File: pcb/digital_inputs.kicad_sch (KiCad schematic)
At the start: 9 parts, among them CN3 VL0831510000G, U2 ISO1212, U4 ISO1212

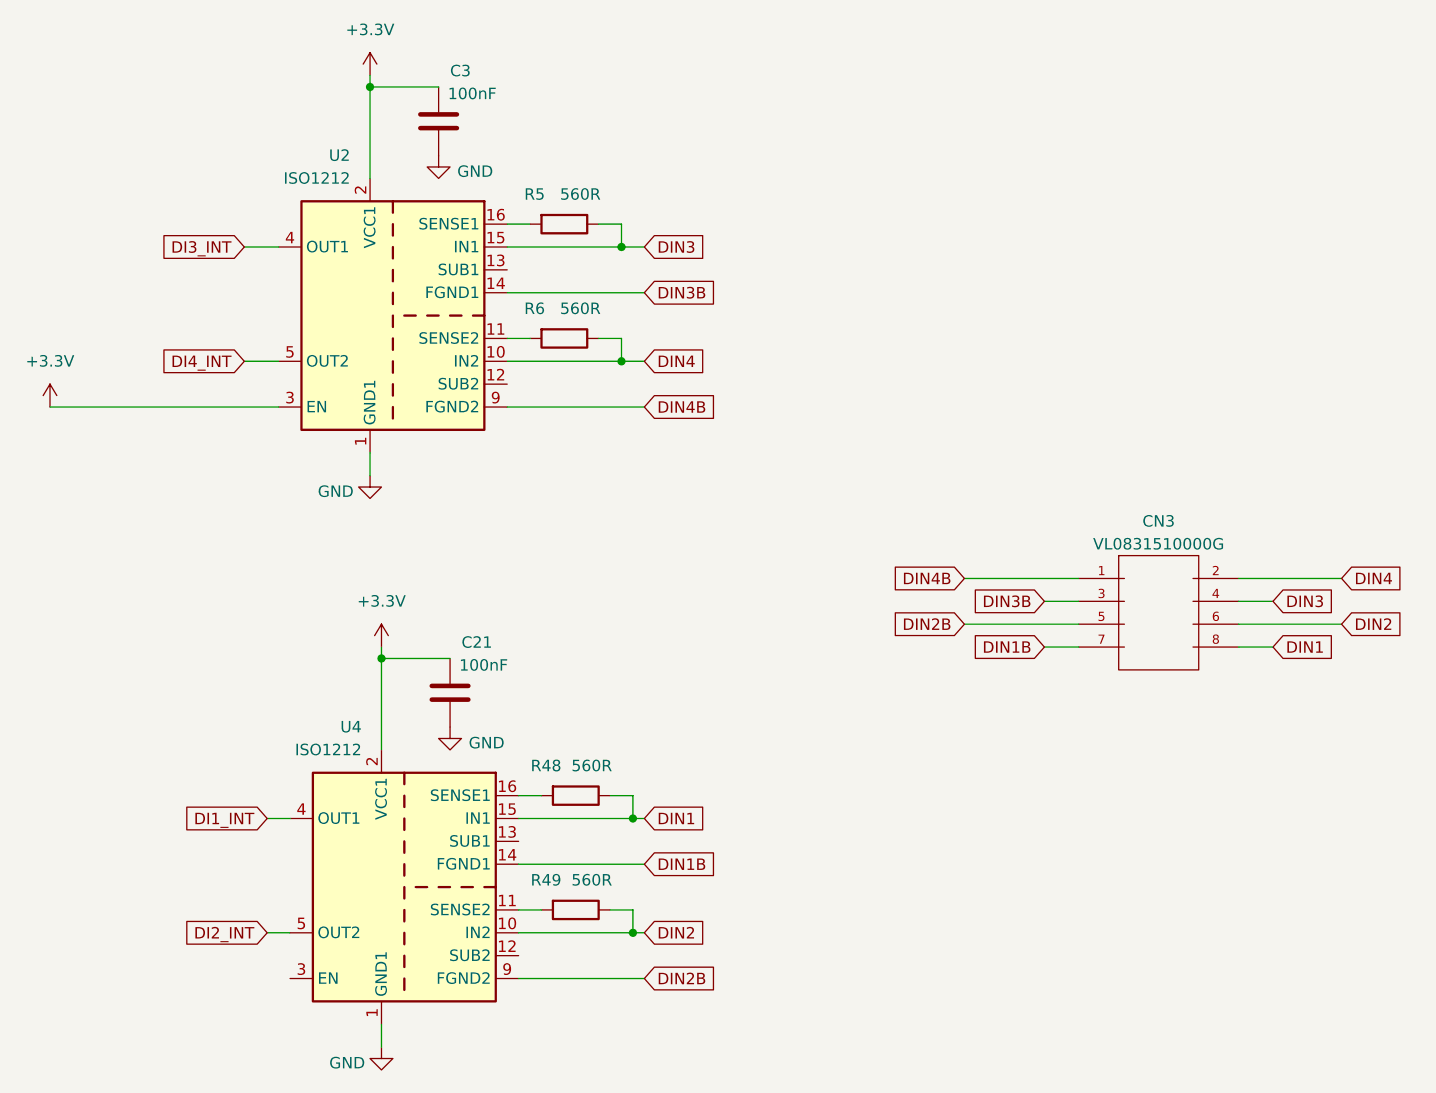
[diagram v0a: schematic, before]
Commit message: Added recommended threshold resistor and capacitor to all digital inputs, as recommended in the ISO1212 datasheet.
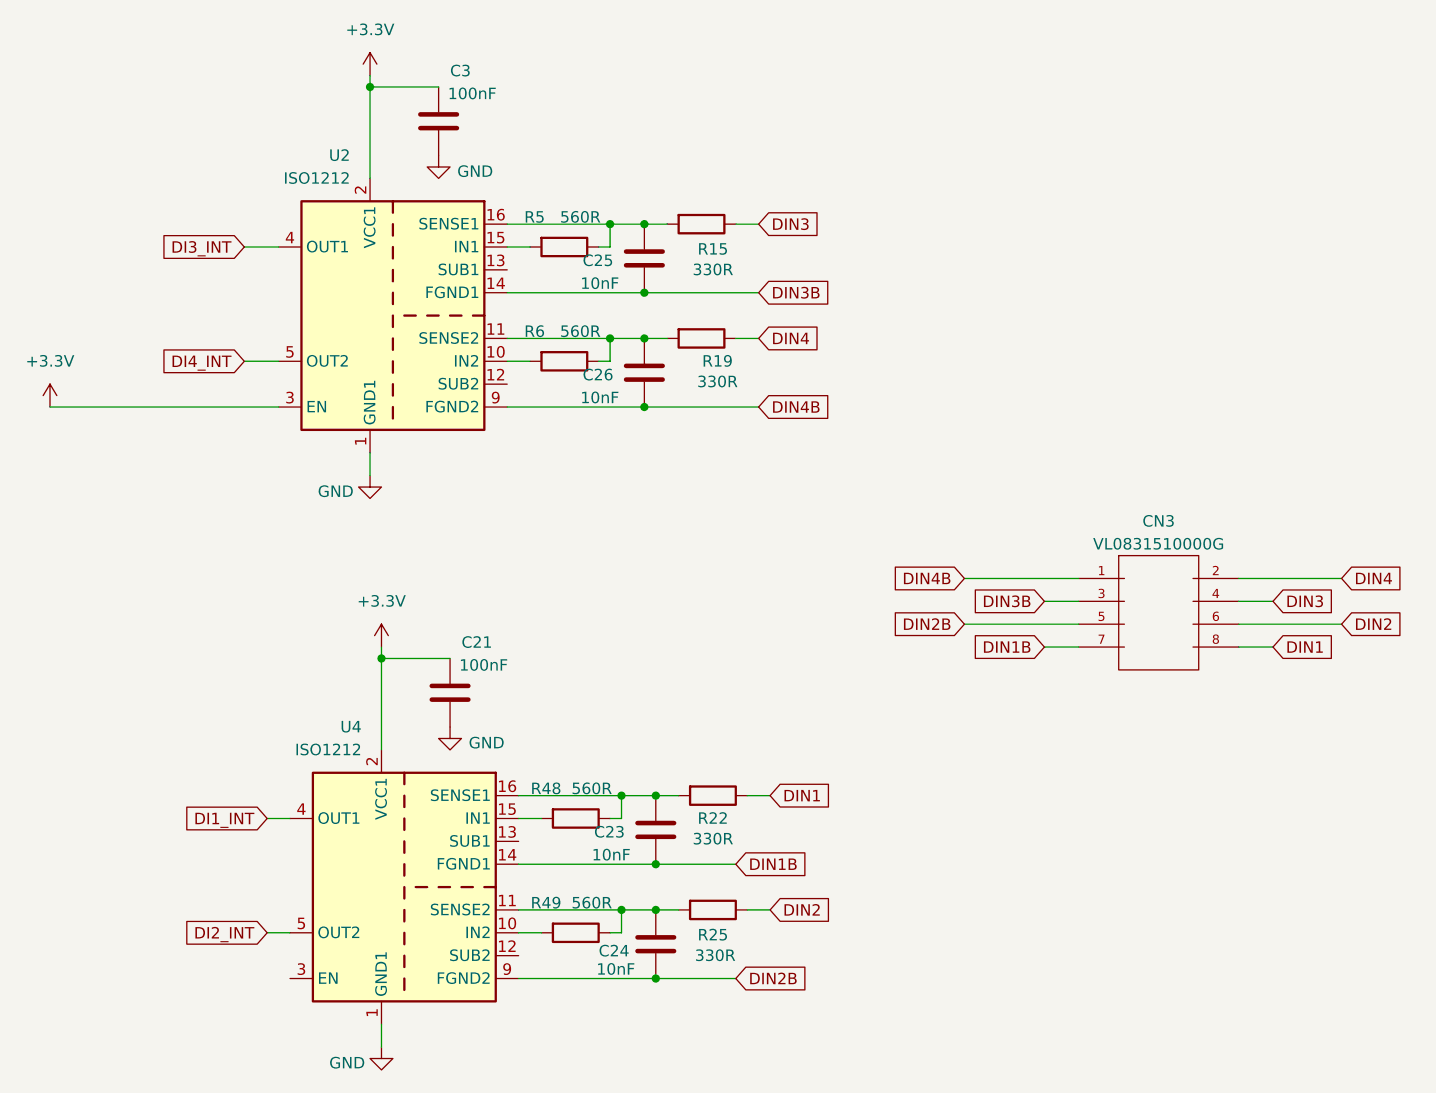
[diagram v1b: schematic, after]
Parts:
- added C23, C24, C25, C26: 10nF, Capacitor_SMD:C_0805_2012Metric, symbol Device:C
- added R15, R19, R22, R25: 330R, Resistor_SMD:R_0805_2012Metric, symbol Device:R
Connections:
- net DIN1: now also R22.1; no longer R48.1, U4.15 (IN1)
- net DIN1B: now also C23.2
- net DIN2: now also R25.1; no longer R49.1, U4.10 (IN2)
- net DIN2B: now also C24.2
- net DIN3: now also R15.1; no longer R5.1, U2.15 (IN1)
- net DIN3B: now also C25.2
- net DIN4: now also R19.1; no longer R6.1, U2.10 (IN2)
- net DIN4B: now also C26.2
- net at U4.16 (SENSE1): now also R48.1, C23.1, R22.2; no longer R48.2
- net at U2.16 (SENSE1): now also R5.1, C25.1, R15.2; no longer R5.2
- net at U4.11 (SENSE2): now also R49.1, C24.1, R25.2; no longer R49.2
- net at U2.11 (SENSE2): now also R6.1, C26.1, R19.2; no longer R6.2
- new net: R48.2, U4.15 (IN1)
- new net: R5.2, U2.15 (IN1)
- new net: R49.2, U4.10 (IN2)
- new net: R6.2, U2.10 (IN2)
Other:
- moved on the sheet: R48, R49, R5, R6
